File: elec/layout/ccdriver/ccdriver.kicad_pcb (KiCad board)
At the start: 2 copper layers, 25.4 x 14.8 mm, 31 parts, among them U1 ?, U2 ?, U3 ?, U4 ?, U5 ?, U6 ?, U7 ?

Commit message: new step models
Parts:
- R7: value 62.5mW Thick Film Resistors 50V ±1% 300mΩ 0402 Chip Resistor - Surface Mount ROHS -> 100mW 300mΩ Chip Splitter 0ppm/℃~+300ppm/℃ ±1% 0201 Current Sense Resistors / Shunt Resistors ROHS; footprint lib:R0402 -> lib:R0201
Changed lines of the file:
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@@
 		)
 	)
-	(footprint "lib:R0402"
+	(footprint "lib:R0201"
 		(layer "F.Cu")
 		(at 184.4 114.2)
-		(descr "Resistor SMD 0402 (1005 Metric), square (rectangular) end terminal, IPC_7351 nominal, (Body size source: IPC-SM-782 page 72, https://www.pcb-3d.com/wordpress/wp-content/uploads/ipc-sm-782a_amendment_1_and_2.pdf), generated with kicad-footprint-generator")
+		(descr "Resistor SMD 0201 (0603 Metric), square (rectangular) end terminal, IPC_7351 nominal, (Body size source: https://www.vishay.com/docs/20052/crcw0201e3.pdf), generated with kicad-footprint-generator")
 		(tags "resistor")
 		(property "Reference" "R7"
-			(at 0 -1.17 0)
+			(at 0 -1.05 0)
 			(layer "F.SilkS")
 			(effects
@@
 			)
 		)
-		(property "Value" "62.5mW Thick Film Resistors 50V ±1% 300mΩ 0402  Chip Resistor - Surface Mount ROHS"
-			(at 0 1.17 0)
+		(property "Value" "100mW 300mΩ Chip Splitter 0ppm/℃~+300ppm/℃ ±1% 0201  Current Sense Resistors / Shunt Resistors ROHS"
+			(at 0 1.05 0)
 			(layer "F.Fab")
 			(effects
@@
 		(attr smd)
 		(fp_line
-			(start -0.153641 -0.38)
-			(end 0.153641 -0.38)
-			(stroke
-				(width 0.12)
-				(type solid)
-			)
-			(layer "F.SilkS")
-		)
-		(fp_line
-			(start -0.153641 0.38)
-			(end 0.153641 0.38)
-			(stroke
-				(width 0.12)
-				(type solid)
-			)
-			(layer "F.SilkS")
-		)
-		(fp_line
-			(start -0.93 -0.47)
-			(end 0.93 -0.47)
+			(start -0.7 -0.35)
+			(end 0.7 -0.35)
 			(stroke
 				(width 0.05)
@@
 		)
 		(fp_line
-			(start -0.93 0.47)
-			(end -0.93 -0.47)
+			(start -0.7 0.35)
+			(end -0.7 -0.35)
 			(stroke
 				(width 0.05)
@@
 		)
 		(fp_line
-			(start 0.93 -0.47)
-			(end 0.93 0.47)
+			(start 0.7 -0.35)
+			(end 0.7 0.35)
 			(stroke
 				(width 0.05)
@@
 		)
 		(fp_line
-			(start 0.93 0.47)
-			(end -0.93 0.47)
+			(start 0.7 0.35)
+			(end -0.7 0.35)
 			(stroke
 				(width 0.05)
@@
 		)
 		(fp_line
-			(start -0.525 -0.27)
-			(end 0.525 -0.27)
+			(start -0.3 -0.15)
+			(end 0.3 -0.15)
 			(stroke
 				(width 0.1)
@@
 		)
 		(fp_line
-			(start -0.525 0.27)
-			(end -0.525 -0.27)
+			(start -0.3 0.15)
+			(end -0.3 -0.15)
 			(stroke
 				(width 0.1)
@@
 		)
 		(fp_line
-			(start 0.525 -0.27)
-			(end 0.525 0.27)
+			(start 0.3 -0.15)
+			(end 0.3 0.15)
 			(stroke
 				(width 0.1)
@@
 		)
 		(fp_line
-			(start 0.525 0.27)
-			(end -0.525 0.27)
+			(start 0.3 0.15)
+			(end -0.3 0.15)
 			(stroke
 				(width 0.1)
@@
 		)
 		(fp_text user "${REFERENCE}"
-			(at 0 0 0)
+			(at 0 -0.68 0)
 			(layer "F.Fab")
 			(effects
 				(font
-					(size 0.26 0.26)
+					(size 0.25 0.25)
 					(thickness 0.04)
 				)
 			)
 		)
+		(pad "" smd roundrect
+			(at -0.345 0)
+			(size 0.318 0.36)
+			(layers "F.Paste")
+			(roundrect_rratio 0.25)
+		)
+		(pad "" smd roundrect
+			(at 0.345 0)
+			(size 0.318 0.36)
+			(layers "F.Paste")
+			(roundrect_rratio 0.25)
+		)
 		(pad "1" smd roundrect
-			(at -0.51 0)
-			(size 0.54 0.64)
-			(layers "F.Cu" "F.Paste" "F.Mask")
+			(at -0.32 0)
+			(size 0.46 0.4)
+			(layers "F.Cu" "F.Mask")
 			(roundrect_rratio 0.25)
 			(net 18 "fb")
@@
 		)
 		(pad "2" smd roundrect
-			(at 0.51 0)
-			(size 0.54 0.64)
-			(layers "F.Cu" "F.Paste" "F.Mask")
+			(at 0.32 0)
+			(size 0.46 0.4)
+			(layers "F.Cu" "F.Mask")
 			(roundrect_rratio 0.25)
 			(net 36 "gnd")
 			(pintype "stereo")
 		)
-		(model "${KICAD6_3DMODEL_DIR}/Resistor_SMD.3dshapes/R_0402_1005Metric.wrl"
+		(model "${KICAD6_3DMODEL_DIR}/Resistor_SMD.3dshapes/R_0201_0603Metric.wrl"
 			(offset
 				(xyz 0 0 0)
@@
 			(pintype "stereo")
 		)
-		(model "/home/lucy/atopile_projects/uv-lamp/build/footprints/footprints.3dshapes/R0201_L0.6-W0.3-H0.3.step"
+		(model "/home/lucy/Documents/atopile/uv-lamp/elec/footprints/footprints.3dshapes/R0201_L0.6-W0.3-H0.3.wrl"
 			(offset
 				(xyz 0 -0 0)
@@
 			(pintype "stereo")
 		)
-		(model "/home/lucy/atopile_projects/uv-lamp/build/footprints/footprints.3dshapes/R0201_L0.6-W0.3-H0.3.step"
+		(model "/home/lucy/Documents/atopile/uv-lamp/elec/footprints/footprints.3dshapes/R0201_L0.6-W0.3-H0.3.step"
 			(offset
 				(xyz 0 -0 0)
@@
 			(pintype "stereo")
 		)
-		(model "/home/lucy/atopile_projects/uv-lamp/build/footprints/footprints.3dshapes/R0201_L0.6-W0.3-H0.3.step"
+		(model "/home/lucy/Documents/atopile/uv-lamp/elec/footprints/footprints.3dshapes/R0201_L0.6-W0.3-H0.3.wrl"
 			(offset
 				(xyz 0 -0 0)
@@
 			(pintype "stereo")
 		)
-		(model "/home/lucy/atopile_projects/uv-lamp/build/footprints/footprints.3dshapes/R0201_L0.6-W0.3-H0.3.step"
+		(model "/home/lucy/Documents/atopile/uv-lamp/elec/footprints/footprints.3dshapes/R0201_L0.6-W0.3-H0.3.wrl"
 			(offset
-				(xyz -0 -0 0)
+				(xyz 0 0 0)
 			)
 			(scale
@@
 	)
 	(segment
-		(start 189.45 118.55)
-		(end 189.367893 118.55)
+		(start 189.367893 118.55)
+		(end 189.067893 118.25)
 		(width 0.2)
 		(layer "B.Cu")
@@
 	)
 	(segment
-		(start 189.367893 118.55)
-		(end 189.017893 118.2)
+		(start 179 118.25)
+		(end 175.25 114.5)
 		(width 0.2)
 		(layer "B.Cu")
@@
 	)
 	(segment
-		(start 189.017893 118.2)
-		(end 178.95 118.2)
+		(start 189.067893 118.25)
+		(end 179 118.25)
 		(width 0.2)
 		(layer "B.Cu")
@@
 	)
 	(segment
-		(start 178.95 118.2)
-		(end 175.25 114.5)
+		(start 189.45 118.55)
+		(end 189.367893 118.55)
 		(width 0.2)
 		(layer "B.Cu")
@@
 	)
 	(via
+		(at 177.75 118.25)
+		(size 0.8)
+		(drill 0.4)
+		(layers "F.Cu" "B.Cu")
+		(net 36)
+	)
+	(via
 		(at 189.891149 114.254269)
 		(size 0.4)
@@
 		(net 36)
 	)
-	(via
-		(at 177.672653 118.072653)
-		(size 0.8)
-		(drill 0.4)
-		(layers "F.Cu" "B.Cu")
-		(net 36)
-	)

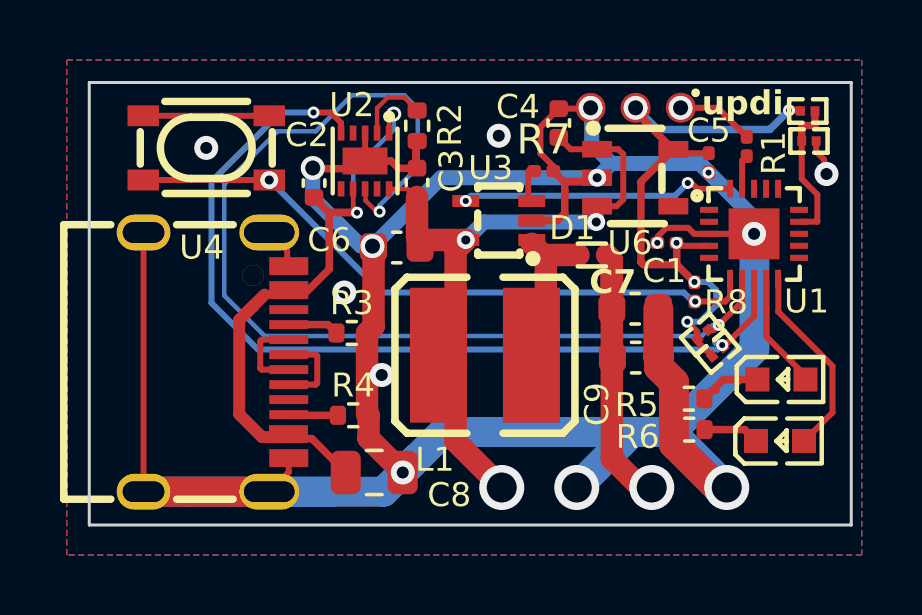
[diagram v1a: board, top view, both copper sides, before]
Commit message: changed r7 to 0402
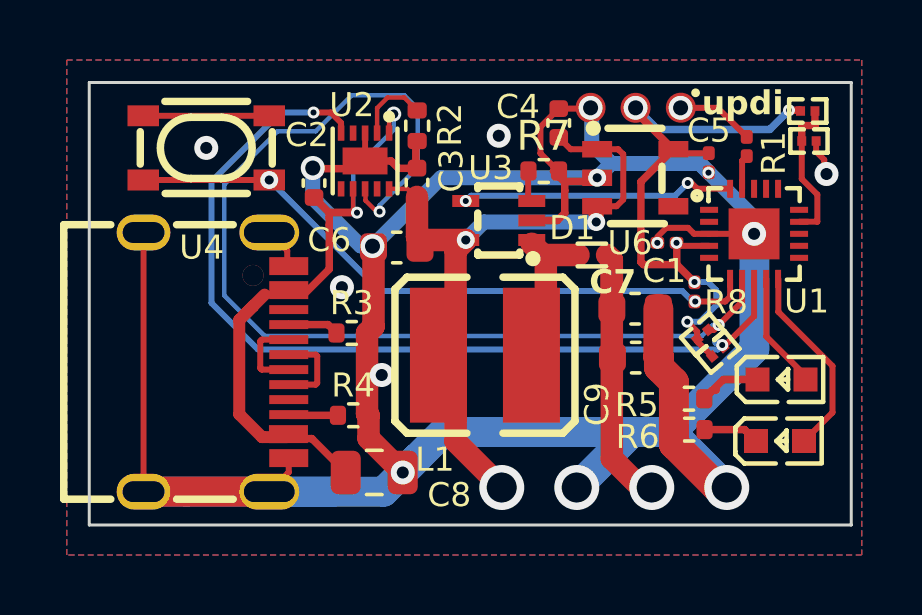
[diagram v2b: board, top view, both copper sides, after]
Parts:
- R7: value 100mW 300mΩ Chip Splitter 0ppm/℃~+300ppm/℃ ±1% 0201 Current Sense Resistors / Shunt Resistors ROHS -> 62.5mW Thick Film Resistors 50V ±1% 300mΩ 0402 Chip Resistor - Surface Mount ROHS; footprint lib:R0201 -> lib:R0402
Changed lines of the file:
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@@
 		)
 	)
-	(footprint "lib:R0201"
+	(footprint "lib:R0402"
 		(layer "F.Cu")
 		(at 184.4 114.2)
-		(descr "Resistor SMD 0201 (0603 Metric), square (rectangular) end terminal, IPC_7351 nominal, (Body size source: https://www.vishay.com/docs/20052/crcw0201e3.pdf), generated with kicad-footprint-generator")
+		(descr "Resistor SMD 0402 (1005 Metric), square (rectangular) end terminal, IPC_7351 nominal, (Body size source: IPC-SM-782 page 72, https://www.pcb-3d.com/wordpress/wp-content/uploads/ipc-sm-782a_amendment_1_and_2.pdf), generated with kicad-footprint-generator")
 		(tags "resistor")
 		(property "Reference" "R7"
-			(at 0 -1.05 0)
+			(at 0 -1.17 0)
 			(layer "F.SilkS")
 			(effects
@@
 			)
 		)
-		(property "Value" "100mW 300mΩ Chip Splitter 0ppm/℃~+300ppm/℃ ±1% 0201  Current Sense Resistors / Shunt Resistors ROHS"
-			(at 0 1.05 0)
+		(property "Value" "62.5mW Thick Film Resistors 50V ±1% 300mΩ 0402  Chip Resistor - Surface Mount ROHS"
+			(at 0 1.17 0)
 			(layer "F.Fab")
 			(effects
@@
 		(attr smd)
 		(fp_line
-			(start -0.7 -0.35)
-			(end 0.7 -0.35)
+			(start -0.153641 -0.38)
+			(end 0.153641 -0.38)
+			(stroke
+				(width 0.12)
+				(type solid)
+			)
+			(layer "F.SilkS")
+		)
+		(fp_line
+			(start -0.153641 0.38)
+			(end 0.153641 0.38)
+			(stroke
+				(width 0.12)
+				(type solid)
+			)
+			(layer "F.SilkS")
+		)
+		(fp_line
+			(start -0.93 -0.47)
+			(end 0.93 -0.47)
 			(stroke
 				(width 0.05)
@@
 		)
 		(fp_line
-			(start -0.7 0.35)
-			(end -0.7 -0.35)
+			(start -0.93 0.47)
+			(end -0.93 -0.47)
 			(stroke
 				(width 0.05)
@@
 		)
 		(fp_line
-			(start 0.7 -0.35)
-			(end 0.7 0.35)
+			(start 0.93 -0.47)
+			(end 0.93 0.47)
 			(stroke
 				(width 0.05)
@@
 		)
 		(fp_line
-			(start 0.7 0.35)
-			(end -0.7 0.35)
+			(start 0.93 0.47)
+			(end -0.93 0.47)
 			(stroke
 				(width 0.05)
@@
 		)
 		(fp_line
-			(start -0.3 -0.15)
-			(end 0.3 -0.15)
+			(start -0.525 -0.27)
+			(end 0.525 -0.27)
 			(stroke
 				(width 0.1)
@@
 		)
 		(fp_line
-			(start -0.3 0.15)
-			(end -0.3 -0.15)
+			(start -0.525 0.27)
+			(end -0.525 -0.27)
 			(stroke
 				(width 0.1)
@@
 		)
 		(fp_line
-			(start 0.3 -0.15)
-			(end 0.3 0.15)
+			(start 0.525 -0.27)
+			(end 0.525 0.27)
 			(stroke
 				(width 0.1)
@@
 		)
 		(fp_line
-			(start 0.3 0.15)
-			(end -0.3 0.15)
+			(start 0.525 0.27)
+			(end -0.525 0.27)
 			(stroke
 				(width 0.1)
@@
 		)
 		(fp_text user "${REFERENCE}"
-			(at 0 -0.68 0)
+			(at 0 0 0)
 			(layer "F.Fab")
 			(effects
 				(font
-					(size 0.25 0.25)
+					(size 0.26 0.26)
 					(thickness 0.04)
 				)
 			)
 		)
-		(pad "" smd roundrect
-			(at -0.345 0)
-			(size 0.318 0.36)
-			(layers "F.Paste")
-			(roundrect_rratio 0.25)
-		)
-		(pad "" smd roundrect
-			(at 0.345 0)
-			(size 0.318 0.36)
-			(layers "F.Paste")
-			(roundrect_rratio 0.25)
-		)
 		(pad "1" smd roundrect
-			(at -0.32 0)
-			(size 0.46 0.4)
-			(layers "F.Cu" "F.Mask")
+			(at -0.51 0)
+			(size 0.54 0.64)
+			(layers "F.Cu" "F.Paste" "F.Mask")
 			(roundrect_rratio 0.25)
 			(net 18 "fb")
@@
 		)
 		(pad "2" smd roundrect
-			(at 0.32 0)
-			(size 0.46 0.4)
-			(layers "F.Cu" "F.Mask")
+			(at 0.51 0)
+			(size 0.54 0.64)
+			(layers "F.Cu" "F.Paste" "F.Mask")
 			(roundrect_rratio 0.25)
 			(net 36 "gnd")
 			(pintype "stereo")
 		)
-		(model "${KICAD6_3DMODEL_DIR}/Resistor_SMD.3dshapes/R_0201_0603Metric.wrl"
+		(model "${KICAD6_3DMODEL_DIR}/Resistor_SMD.3dshapes/R_0402_1005Metric.wrl"
 			(offset
 				(xyz 0 0 0)
@@
 			(pintype "stereo")
 		)
-		(model "/home/lucy/Documents/atopile/uv-lamp/elec/footprints/footprints.3dshapes/R0201_L0.6-W0.3-H0.3.wrl"
+		(model "/home/lucy/atopile_projects/uv-lamp/build/footprints/footprints.3dshapes/R0201_L0.6-W0.3-H0.3.step"
 			(offset
 				(xyz 0 -0 0)
@@
 			(pintype "stereo")
 		)
-		(model "/home/lucy/Documents/atopile/uv-lamp/elec/footprints/footprints.3dshapes/R0201_L0.6-W0.3-H0.3.step"
+		(model "/home/lucy/atopile_projects/uv-lamp/build/footprints/footprints.3dshapes/R0201_L0.6-W0.3-H0.3.step"
 			(offset
 				(xyz 0 -0 0)
@@
 			(pintype "stereo")
 		)
-		(model "/home/lucy/Documents/atopile/uv-lamp/elec/footprints/footprints.3dshapes/R0201_L0.6-W0.3-H0.3.wrl"
+		(model "/home/lucy/atopile_projects/uv-lamp/build/footprints/footprints.3dshapes/R0201_L0.6-W0.3-H0.3.step"
 			(offset
 				(xyz 0 -0 0)
@@
 			(pintype "stereo")
 		)
-		(model "/home/lucy/Documents/atopile/uv-lamp/elec/footprints/footprints.3dshapes/R0201_L0.6-W0.3-H0.3.wrl"
+		(model "/home/lucy/atopile_projects/uv-lamp/build/footprints/footprints.3dshapes/R0201_L0.6-W0.3-H0.3.step"
 			(offset
-				(xyz 0 0 0)
+				(xyz -0 -0 0)
 			)
 			(scale
@@
 	)
 	(segment
-		(start 189.367893 118.55)
-		(end 189.067893 118.25)
+		(start 189.45 118.55)
+		(end 189.367893 118.55)
 		(width 0.2)
 		(layer "B.Cu")
@@
 	)
 	(segment
-		(start 179 118.25)
-		(end 175.25 114.5)
+		(start 189.367893 118.55)
+		(end 189.017893 118.2)
 		(width 0.2)
 		(layer "B.Cu")
@@
 	)
 	(segment
-		(start 189.067893 118.25)
-		(end 179 118.25)
+		(start 189.017893 118.2)
+		(end 178.95 118.2)
 		(width 0.2)
 		(layer "B.Cu")
@@
 	)
 	(segment
-		(start 189.45 118.55)
-		(end 189.367893 118.55)
+		(start 178.95 118.2)
+		(end 175.25 114.5)
 		(width 0.2)
 		(layer "B.Cu")
@@
 	)
 	(via
-		(at 177.75 118.25)
-		(size 0.8)
-		(drill 0.4)
-		(layers "F.Cu" "B.Cu")
-		(net 36)
-	)
-	(via
 		(at 189.891149 114.254269)
 		(size 0.4)
@@
 		(net 36)
 	)
+	(via
+		(at 177.672653 118.072653)
+		(size 0.8)
+		(drill 0.4)
+		(layers "F.Cu" "B.Cu")
+		(net 36)
+	)
